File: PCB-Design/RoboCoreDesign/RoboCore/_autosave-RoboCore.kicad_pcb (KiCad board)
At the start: 4 copper layers, 68 x 60 mm, 80 parts, among them IC1 DRV8245SQRXZRQ1, IC2 DRV8245SQRXZRQ1, J1 SS-52400-002, J2 B2B-PH-SM4-TB, J3 MOTOR_A, J4 MOTOR_B, Q1 BC817, Q2 BC817, SW1 RESET, SW2 BOOT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

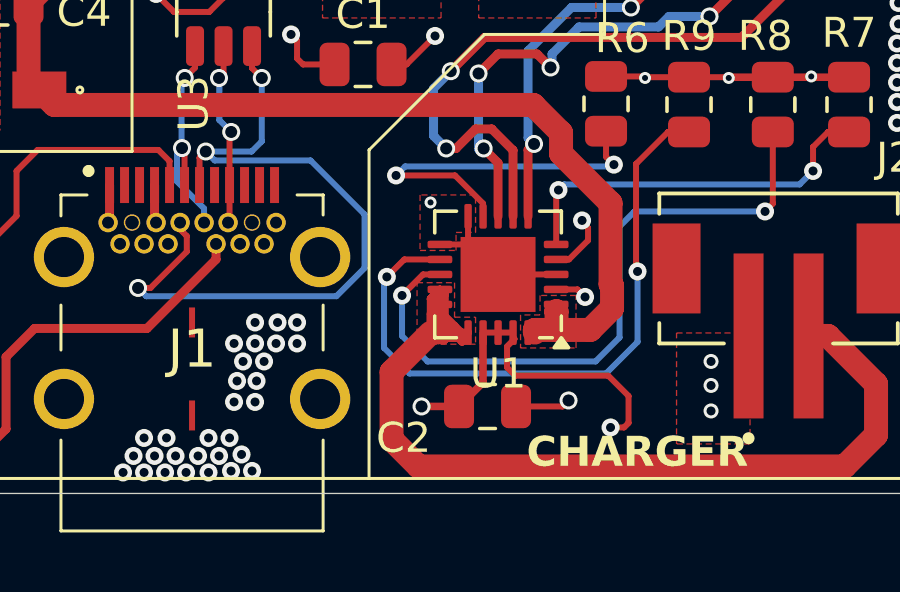
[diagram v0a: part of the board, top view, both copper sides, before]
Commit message: made to finish the component routing
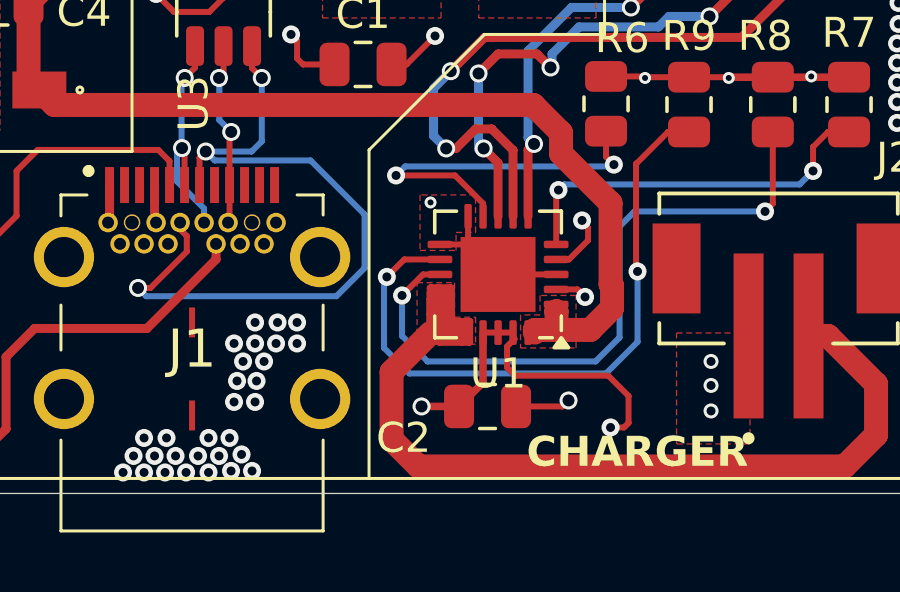
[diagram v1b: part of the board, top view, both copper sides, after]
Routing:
- net /VBAT: track 40.2 -> 49.2 mm
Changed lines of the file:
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@@
+	)
+	(segment
+		(start 128.495 115.83)
+		(end 128.495 116.5)
+		(width 0.254)
+		(layer "F.Cu")
+		(net 51)
 	)
 	(segment
@@
 	)
 	(segment
+		(start 128.497 115.828)
+		(end 128.495 115.83)
+		(width 0.254)
+		(layer "F.Cu")
+		(net 51)
+	)
+	(segment
 		(start 127.45 116.45)
 		(end 127.2 116.2)
@@
 	)
 	(segment
+		(start 127.872 115.828)
+		(end 128 115.828)
+		(width 0.254)
+		(layer "F.Cu")
+		(net 51)
+	)
+	(segment
 		(start 127.997 115.953)
 		(end 127.8845 115.953)
@@
 	)
 	(segment
+		(start 127.2 116.2)
+		(end 127.2 114.85)
+		(width 0.254)
+		(layer "F.Cu")
+		(net 51)
+	)
+	(segment
+		(start 127.4125 114.85)
+		(end 127.2 114.85)
+		(width 0.254)
+		(layer "F.Cu")
+		(net 51)
+	)
+	(segment
 		(start 127.65 116.1875)
 		(end 127.2125 116.1875)
+		(width 0.254)
+		(layer "F.Cu")
+		(net 51)
+	)
+	(segment
+		(start 128.2 115.828)
+		(end 128.2 115.9375)
 		(width 0.254)
 		(layer "F.Cu")
@@
 	)
 	(segment
+		(start 127.2 114.703)
+		(end 127.2 115.5625)
+		(width 0.254)
+		(layer "F.Cu")
+		(net 51)
+	)
+	(segment
+		(start 127.5125 114.75)
+		(end 127.4655 114.703)
+		(width 0.254)
+		(layer "F.Cu")
+		(net 51)
+	)
+	(segment
+		(start 127.4655 114.703)
+		(end 127.872 114.703)
+		(width 0.254)
+		(layer "F.Cu")
+		(net 51)
+	)
+	(segment
 		(start 127.2 116.2)
 		(end 127.2 115.0625)
@@
 		(start 127.5125 114.75)
 		(end 127.5125 115.4685)
+		(width 0.254)
+		(layer "F.Cu")
+		(net 51)
+	)
+	(segment
+		(start 127.872 114.703)
+		(end 127.872 115.65)
 		(width 0.254)
 		(layer "F.Cu")
@@
 	)
 	(segment
+		(start 127.5125 114.75)
+		(end 127.872 114.75)
+		(width 0.254)
+		(layer "F.Cu")
+		(net 51)
+	)
+	(segment
 		(start 128 116.1875)
 		(end 127.65 116.1875)
@@
 	)
 	(segment
+		(start 127.872 114.75)
+		(end 127.872 115.65)
+		(width 0.254)
+		(layer "F.Cu")
+		(net 51)
+	)
+	(segment
 		(start 127.85 116.25)
 		(end 127.85 116.2)
+		(width 0.254)
+		(layer "F.Cu")
+		(net 51)
+	)
+	(segment
+		(start 128.2 115.9375)
+		(end 128.45 116.1875)
 		(width 0.254)
 		(layer "F.Cu")
@@
 	)
 	(segment
+		(start 127.4655 114.703)
+		(end 127.2 114.703)
+		(width 0.254)
+		(layer "F.Cu")
+		(net 51)
+	)
+	(segment
+		(start 127.5125 114.75)
+		(end 127.4125 114.85)
+		(width 0.254)
+		(layer "F.Cu")
+		(net 51)
+	)
+	(segment
 		(start 127.40625 115.70625)
 		(end 127.5125 115.6)
@@
 	)
 	(segment
+		(start 128 115.828)
+		(end 128.2 115.828)
+		(width 0.254)
+		(layer "F.Cu")
+		(net 51)
+	)
+	(segment
 		(start 127.2 115.0625)
 		(end 127.28125 114.98125)
@@
 	)
 	(segment
+		(start 128.495 116.5)
+		(end 127.5 116.5)
+		(width 0.254)
+		(layer "F.Cu")
+		(net 51)
+	)
+	(segment
 		(start 127.2 115.0625)
 		(end 127.5125 114.75)
+		(width 0.254)
+		(layer "F.Cu")
+		(net 51)
+	)
+	(segment
+		(start 127.872 115.65)
+		(end 127.872 115.828)
 		(width 0.254)
 		(layer "F.Cu")
@@
 	)
 	(segment
+		(start 128 115.828)
+		(end 128.497 115.828)
+		(width 0.254)
+		(layer "F.Cu")
+		(net 51)
+	)
+	(segment
 		(start 127.33125 115.43125)
 		(end 127.5125 115.25)
@@
 		(start 127.65 116.45)
 		(end 127.45 116.45)
+		(width 0.254)
+		(layer "F.Cu")
+		(net 51)
+	)
+	(segment
+		(start 127.5 116.5)
+		(end 127.2 116.2)
 		(width 0.254)
 		(layer "F.Cu")
@@
 		(polygon
 			(pts
-				(xy 145.7 104.653847) (xy 150.9 104.65) (xy 151.5 105.15) (xy 151.5 105.15) (xy 157.947206 105.15)
-				(xy 157.502914 105.551974) (xy 158.61056 104.55) (xy 163.05 104.55) (xy 163.05 105.35) (xy 158.65 105.35)
-				(xy 158.35 105.65) (xy 158.35 106.35) (xy 157.9 106.8) (xy 157.7 106.8) (xy 157.65 106.85) (xy 157.65 107.8)
-				(xy 157.675 107.775) (xy 151.628889 107.775) (xy 151.5 107.05) (xy 150.95 106.15) (xy 150.25 105.45)
-				(xy 145.7 105.45)
+				(xy 145.7 104.653847) (xy 150.9 104.65) (xy 151.5 105.15) (xy 157.947206 105.15) (xy 157.502914 105.551974)
+				(xy 158.61056 104.55) (xy 163.05 104.55) (xy 163.05 105.35) (xy 158.65 105.35) (xy 158.35 105.65)
+				(xy 158.35 106.35) (xy 157.9 106.8) (xy 157.7 106.8) (xy 157.65 106.85) (xy 157.65 107.8) (xy 157.675 107.775)
+				(xy 151.628889 107.775) (xy 151.5 107.05) (xy 150.95 106.15) (xy 150.25 105.45) (xy 145.7 105.45)
 			)
 		)
